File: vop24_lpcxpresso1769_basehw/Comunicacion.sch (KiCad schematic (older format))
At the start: 26 parts, among them J301 USB_B_Micro, J302 Conn_01x06_Male, J303 Conn_01x05_Male, J304 Screw_Terminal_01x02, U301 TPD4S014, U302 LTC4411, U303 LT1512

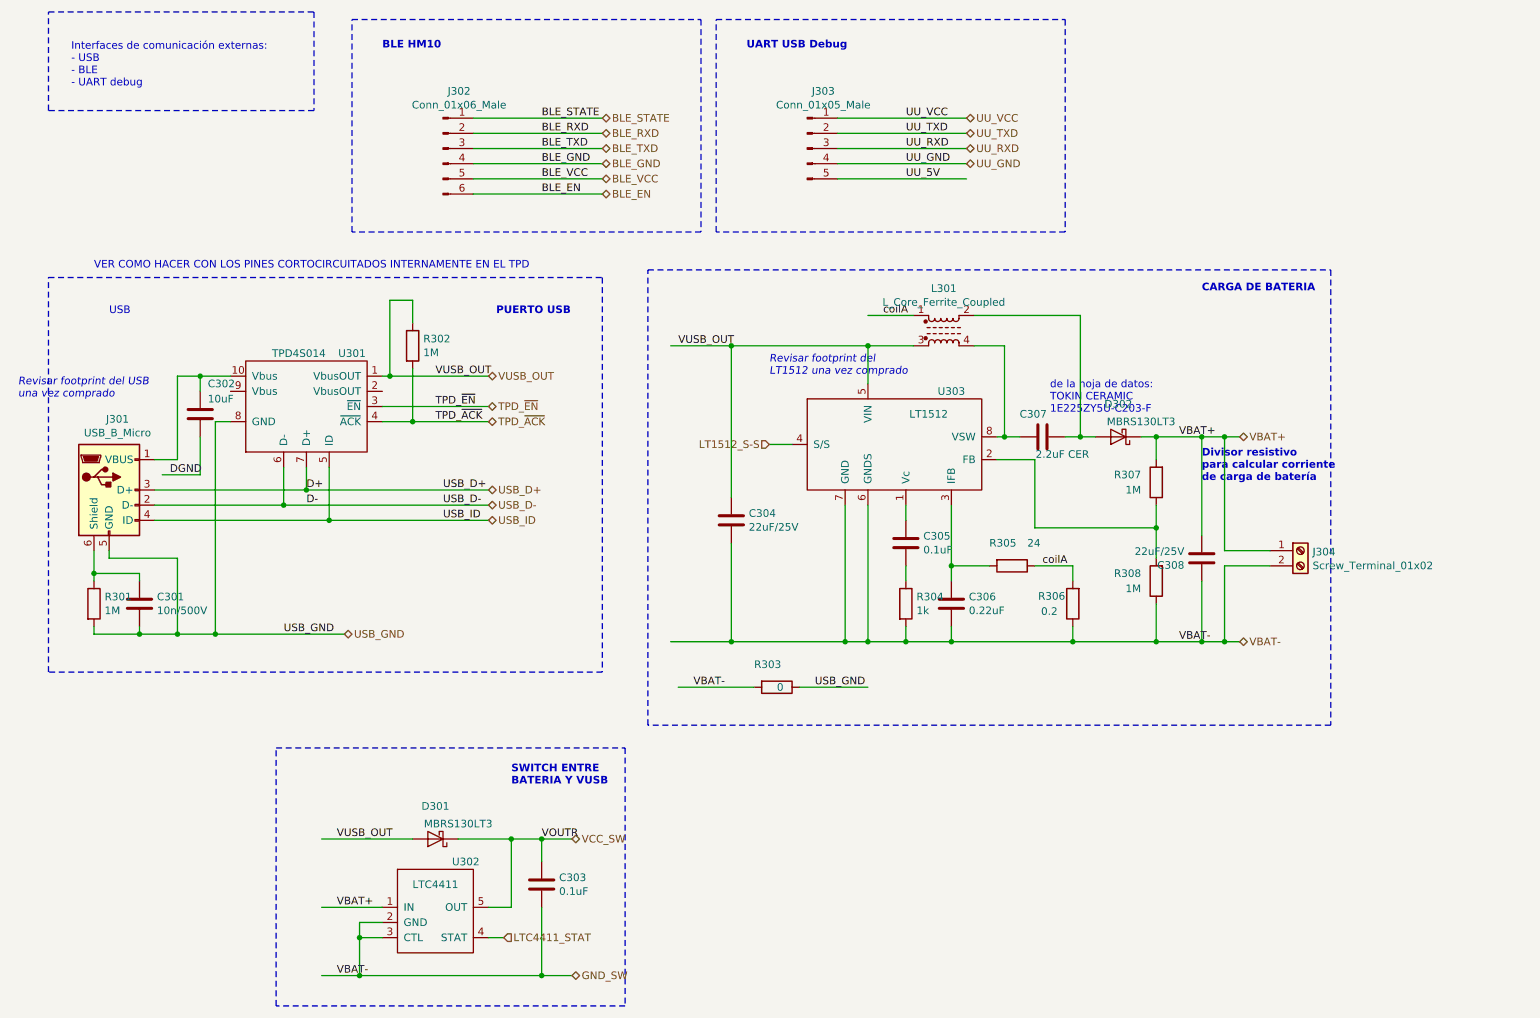
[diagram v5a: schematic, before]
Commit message: Finalizada asociación de todos los footprints. Ver librerías froux-kicad
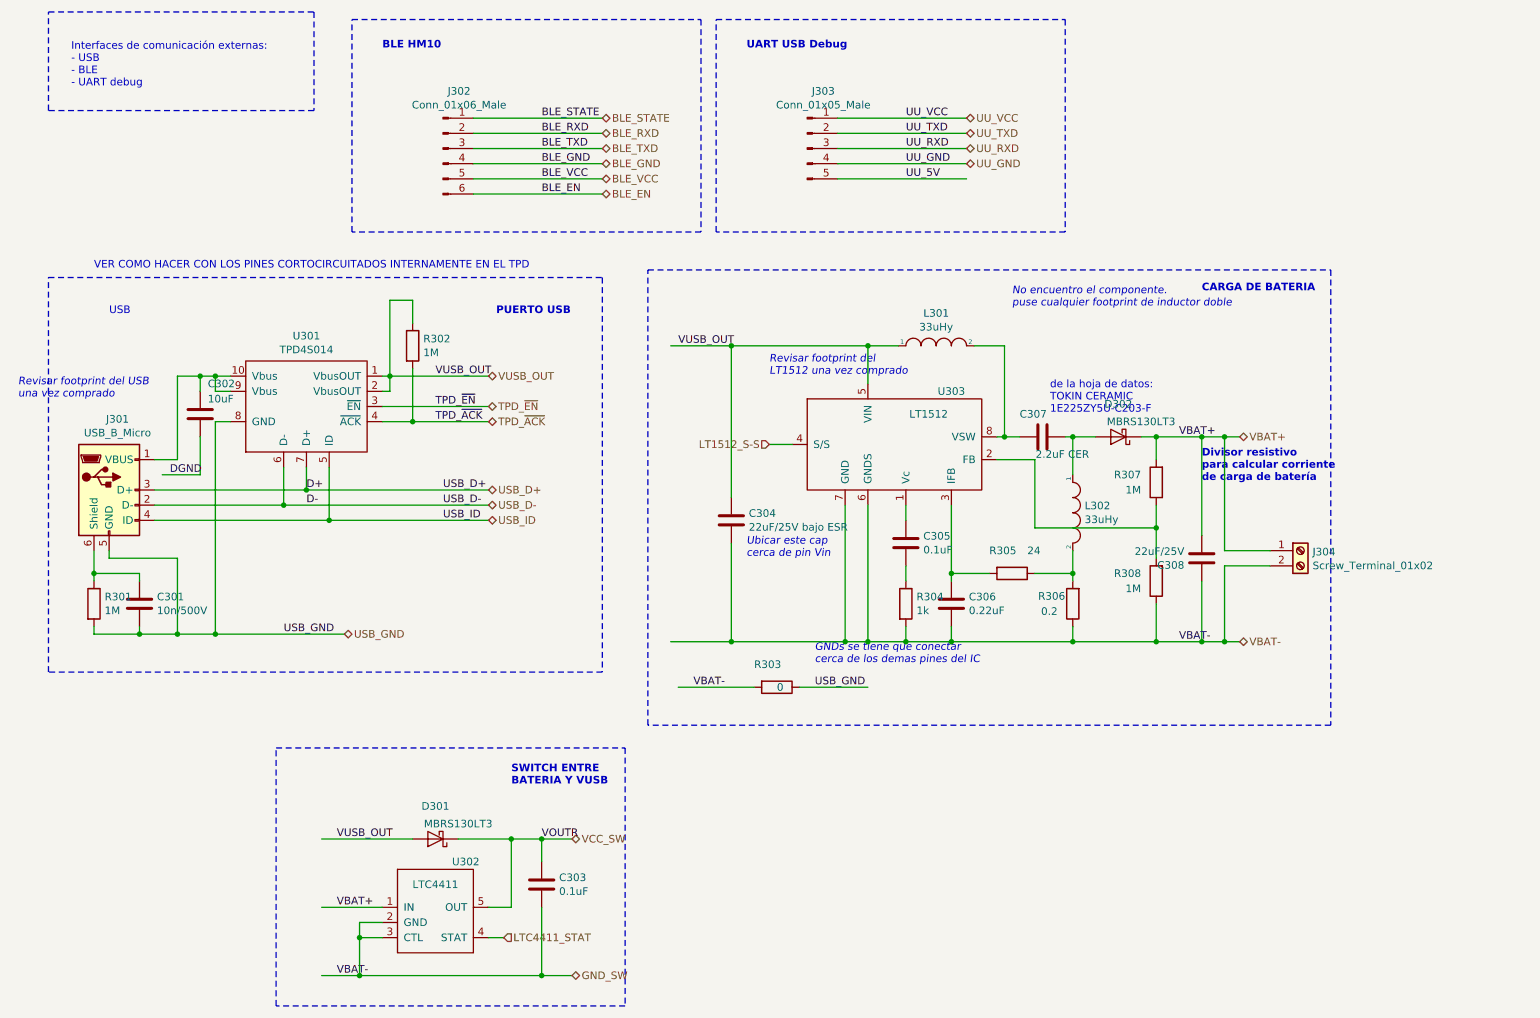
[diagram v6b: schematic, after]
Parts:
- removed L301: L_Core_Ferrite_Coupled, symbol Device:L_Core_Ferrite_Coupled
- added L301, L302: 33uHy, Inductor_THT:L_Radial_D8.7mm_P5.00mm_Fastron_07HCP, symbol pspice:INDUCTOR
- C301, C302, C303, C305, C306: footprint (none) -> Capacitor_SMD:C_0805_2012Metric_Pad1.15x1.40mm_HandSolder
- C304: value 22uF/25V -> 22uF/25V bajo ESR; footprint (none) -> Capacitor_THT:CP_Radial_D5.0mm_P2.50mm
- C307, C308: footprint (none) -> Capacitor_THT:CP_Radial_D5.0mm_P2.50mm
- D302: footprint (none) -> Diode_SMD:D_SMB-SMC_Universal_Handsoldering
- J302: footprint (none) -> Connector_PinHeader_1.27mm:PinHeader_1x06_P1.27mm_Vertical
- J303: footprint (none) -> Connector_PinHeader_1.27mm:PinHeader_1x05_P1.27mm_Vertical
- J304: footprint (none) -> TerminalBlock:TerminalBlock_bornier-2_P5.08mm
- R301, R302, R303, R304, R305, R306, R307, R308: footprint (none) -> Resistor_SMD:R_0805_2012Metric_Pad1.15x1.40mm_HandSolder
- U301: footprint Package_SON:Texas_S-PWSON-N10 -> meport_kicad_libs:Texas_R-PWSON-N10
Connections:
- net labels removed: coilA
- wire segments 125 -> 129
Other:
- note added: "GNDs se tiene que conectar\ncerca de los demas pines del IC"
- note added: "No encuentro el componente.\npuse cualquier footprint de inductor doble"
- note added: "Ubicar este cap\ncerca de pin Vin"
- moved on the sheet: R305
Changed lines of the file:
@@
 F 0 "R301" H 1070 4596 50  0000 L CNN
 F 1 "1M" H 1070 4505 50  0000 L CNN
-F 2 "" V 930 4550 50  0001 C CNN
+F 2 "Resistor_SMD:R_0805_2012Metric_Pad1.15x1.40mm_HandSolder" V 930 4550 50  0001 C CNN
 F 3 "~" H 1000 4550 50  0001 C CNN
 	1    1000 4550
@@
 F 0 "C301" H 1415 4596 50  0000 L CNN
 F 1 "10n/500V" H 1415 4505 50  0000 L CNN
-F 2 "" H 1338 4400 50  0001 C CNN
+F 2 "Capacitor_SMD:C_0805_2012Metric_Pad1.15x1.40mm_HandSolder" H 1338 4400 50  0001 C CNN
 F 3 "~" H 1300 4550 50  0001 C CNN
 	1    1300 4550
@@
 F 0 "J302" H 3406 1928 50  0000 C CNN
 F 1 "Conn_01x06_Male" H 3406 1837 50  0000 C CNN
-F 2 "" H 3300 1550 50  0001 C CNN
+F 2 "Connector_PinHeader_1.27mm:PinHeader_1x06_P1.27mm_Vertical" H 3300 1550 50  0001 C CNN
 F 3 "~" H 3300 1550 50  0001 C CNN
 	1    3300 1550
@@
 F 3 "~" H 1250 3750 50  0001 C CNN
 	1    1100 3800
-	1    0    0    -1
-$EndComp
-$Comp
-L tpd4s014:TPD4S014 U301
-U 1 1 5BAE3ACE
-P 2400 3250
-F 0 "U301" H 2700 3600 50  0000 C CNN
-F 1 "TPD4S014" H 2350 3600 50  0000 C CNN
-F 2 "Package_SON:Texas_S-PWSON-N10" H 2250 3250 50  0001 C CNN
-F 3 "/home/froux/Dropbox/VOP24/docs y hojas de datos/otros/cosas modulo usb/tpd4s014.pdf" H 2250 3250 50  0001 C CNN
-	1    2400 3250
 	1    0    0    -1
 $EndComp
@@
 F 0 "J303" H 5806 1928 50  0000 C CNN
 F 1 "Conn_01x05_Male" H 5806 1837 50  0000 C CNN
-F 2 "" H 5700 1550 50  0001 C CNN
+F 2 "Connector_PinHeader_1.27mm:PinHeader_1x05_P1.27mm_Vertical" H 5700 1550 50  0001 C CNN
 F 3 "~" H 5700 1550 50  0001 C CNN
 	1    5700 1550
@@
 F 0 "R302" H 3170 2896 50  0000 L CNN
 F 1 "1M" H 3170 2805 50  0000 L CNN
-F 2 "" V 3030 2850 50  0001 C CNN
+F 2 "Resistor_SMD:R_0805_2012Metric_Pad1.15x1.40mm_HandSolder" V 3030 2850 50  0001 C CNN
 F 3 "~" H 3100 2850 50  0001 C CNN
 	1    3100 2850
@@
 P 5200 4000
 F 0 "C304" H 5315 4046 50  0000 L CNN
-F 1 "22uF/25V" H 5315 3955 50  0000 L CNN
-F 2 "" H 5238 3850 50  0001 C CNN
+F 1 "22uF/25V bajo ESR" H 5315 3955 50  0000 L CNN
+F 2 "Capacitor_THT:CP_Radial_D5.0mm_P2.50mm" H 5238 3850 50  0001 C CNN
 F 3 "~" H 5200 4000 50  0001 C CNN
 	1    5200 4000
@@
 F 0 "C305" H 6465 4196 50  0000 L CNN
 F 1 "0.1uF" H 6465 4105 50  0000 L CNN
-F 2 "" H 6388 4000 50  0001 C CNN
+F 2 "Capacitor_SMD:C_0805_2012Metric_Pad1.15x1.40mm_HandSolder" H 6388 4000 50  0001 C CNN
 F 3 "~" H 6350 4150 50  0001 C CNN
 	1    6350 4150
@@
 F 0 "C306" H 6765 4596 50  0000 L CNN
 F 1 "0.22uF" H 6765 4505 50  0000 L CNN
-F 2 "" H 6688 4400 50  0001 C CNN
+F 2 "Capacitor_SMD:C_0805_2012Metric_Pad1.15x1.40mm_HandSolder" H 6688 4400 50  0001 C CNN
 F 3 "~" H 6650 4550 50  0001 C CNN
 	1    6650 4550
@@
 F 0 "C307" V 7100 3300 50  0000 L CNN
 F 1 "2.2uF CER" V 7365 3405 50  0000 L CNN
-F 2 "" H 7288 3300 50  0001 C CNN
+F 2 "Capacitor_THT:CP_Radial_D5.0mm_P2.50mm" H 7288 3300 50  0001 C CNN
 F 3 "~" H 7250 3450 50  0001 C CNN
 	1    7250 3450
@@
 F 0 "C308" H 8415 4296 50  0000 L CNN
 F 1 "22uF/25V" H 8415 4205 50  0000 L CNN
-F 2 "" H 8338 4100 50  0001 C CNN
+F 2 "Capacitor_THT:CP_Radial_D5.0mm_P2.50mm" H 8338 4100 50  0001 C CNN
 F 3 "~" H 8300 4250 50  0001 C CNN
 	1    8300 4250
@@
 F 0 "R304" H 6420 4596 50  0000 L CNN
 F 1 "1k" H 6420 4505 50  0000 L CNN
-F 2 "" V 6280 4550 50  0001 C CNN
+F 2 "Resistor_SMD:R_0805_2012Metric_Pad1.15x1.40mm_HandSolder" V 6280 4550 50  0001 C CNN
 F 3 "~" H 6350 4550 50  0001 C CNN
 	1    6350 4550
@@
 F 0 "R306" H 7500 4500 50  0000 L CNN
 F 1 "0.2" H 7550 4600 50  0000 L CNN
-F 2 "" V 7380 4550 50  0001 C CNN
+F 2 "Resistor_SMD:R_0805_2012Metric_Pad1.15x1.40mm_HandSolder" V 7380 4550 50  0001 C CNN
 F 3 "~" H 7450 4550 50  0001 C CNN
 	1    7450 4550
@@
 L Device:R R305
 U 1 1 5BC35500
-P 7050 4300
-F 0 "R305" V 6900 4150 50  0000 L CNN
-F 1 "24" V 6900 4400 50  0000 L CNN
-F 2 "" V 6980 4300 50  0001 C CNN
-F 3 "~" H 7050 4300 50  0001 C CNN
-	1    7050 4300
+P 7050 4350
+F 0 "R305" V 6900 4200 50  0000 L CNN
+F 1 "24" V 6900 4450 50  0000 L CNN
+F 2 "Resistor_SMD:R_0805_2012Metric_Pad1.15x1.40mm_HandSolder" V 6980 4350 50  0001 C CNN
+F 3 "~" H 7050 4350 50  0001 C CNN
+	1    7050 4350
 	0    1    1    0
 $EndComp
@@
 F 0 "R307" H 8100 3700 50  0000 L CNN
 F 1 "1M" H 8100 3800 50  0000 L CNN
-F 2 "" V 7930 3750 50  0001 C CNN
+F 2 "Resistor_SMD:R_0805_2012Metric_Pad1.15x1.40mm_HandSolder" V 7930 3750 50  0001 C CNN
 F 3 "~" H 8000 3750 50  0001 C CNN
 	1    8000 3750
@@
 F 0 "R308" H 8100 4350 50  0000 L CNN
 F 1 "1M" H 8100 4450 50  0000 L CNN
-F 2 "" V 7930 4400 50  0001 C CNN
+F 2 "Resistor_SMD:R_0805_2012Metric_Pad1.15x1.40mm_HandSolder" V 7930 4400 50  0001 C CNN
 F 3 "~" H 8000 4400 50  0001 C CNN
 	1    8000 4400
@@
 Text Notes 8300 3750 0    50   ~ 10
 Divisor resistivo\npara calcular corriente\nde carga de batería
-$Comp
-L Device:L_Core_Ferrite_Coupled L301
-U 1 1 5BC35BED
-P 6600 2750
-F 0 "L301" H 6600 3028 50  0000 C CNN
-F 1 "L_Core_Ferrite_Coupled" H 6600 2937 50  0000 C CNN
-F 2 "" H 6600 2750 50  0001 C CNN
-F 3 "~" H 6600 2750 50  0001 C CNN
-	1    6600 2750
-	1    0    0    -1
-$EndComp
-Wire Wire Line
-	6400 2850 6100 2850
+Wire Wire Line
+	6300 2850 6100 2850
 Wire Wire Line
 	5200 2850 5200 3850
@@
 	6350 4400 6350 4300
 Wire Wire Line
-	6650 4400 6650 4300
-Wire Wire Line
-	6650 4300 6900 4300
-Connection ~ 6650 4300
-Wire Wire Line
-	6650 4300 6650 3900
-Wire Wire Line
-	7200 4300 7450 4300
-Wire Wire Line
-	7450 4300 7450 4400
+	6650 4400 6650 4350
+Wire Wire Line
+	6650 4350 6900 4350
+Connection ~ 6650 4350
+Wire Wire Line
+	6650 4350 6650 3900
+Wire Wire Line
+	7200 4350 7450 4350
+Wire Wire Line
+	7450 4350 7450 4400
 Wire Wire Line
 	8000 4250 8000 4050
@@
 	8000 4050 8000 3900
 Wire Wire Line
-	6800 2650 7500 2650
-Wire Wire Line
-	7500 3450 7400 3450
-Wire Wire Line
-	7500 2650 7500 3450
-Wire Wire Line
 	7450 4800 8000 4800
 Wire Wire Line
@@
 Wire Wire Line
 	8000 4800 8300 4800
-Wire Wire Line
-	6400 2650 6100 2650
-Text Label 6200 2650 0    50   ~ 0
-coilA
-Text Label 7250 4300 0    50   ~ 0
-coilA
 $Comp
 L Device:D_Schottky D302
@@
 F 0 "D302" H 7750 3234 50  0000 C CNN
 F 1 "MBRS130LT3" H 7600 3350 50  0000 C CNN
-F 2 "" H 7750 3450 50  0001 C CNN
+F 2 "Diode_SMD:D_SMB-SMC_Universal_Handsoldering" H 7750 3450 50  0001 C CNN
 F 3 "~" H 7750 3450 50  0001 C CNN
 	1    7750 3450
 	-1   0    0    1
 $EndComp
-Wire Wire Line
-	7600 3450 7500 3450
-Connection ~ 7500 3450
 Wire Wire Line
 	7900 3450 8000 3450
@@
 F 0 "C303" H 4065 6446 50  0000 L CNN
 F 1 "0.1uF" H 4065 6355 50  0000 L CNN
-F 2 "" H 3988 6250 50  0001 C CNN
+F 2 "Capacitor_SMD:C_0805_2012Metric_Pad1.15x1.40mm_HandSolder" H 3988 6250 50  0001 C CNN
 F 3 "~" H 3950 6400 50  0001 C CNN
 	1    3950 6400
@@
 F 0 "R303" V 5350 4950 50  0000 L CNN
 F 1 "0" V 5500 5100 50  0000 L CNN
-F 2 "" V 5430 5100 50  0001 C CNN
+F 2 "Resistor_SMD:R_0805_2012Metric_Pad1.15x1.40mm_HandSolder" V 5430 5100 50  0001 C CNN
 F 3 "~" H 5500 5100 50  0001 C CNN
 	1    5500 5100
@@
 F 0 "C302" H 1750 3500 50  0000 L CNN
 F 1 "10uF" H 1750 3400 50  0000 L CNN
-F 2 "" H 1738 3150 50  0001 C CNN
+F 2 "Capacitor_SMD:C_0805_2012Metric_Pad1.15x1.40mm_HandSolder" H 1738 3150 50  0001 C CNN
 F 3 "~" H 1700 3300 50  0001 C CNN
 	1    1700 3300
@@
 Connection ~ 1700 3050
 Wire Wire Line
-	1700 3050 1900 3050
+	1700 3050 1800 3050
 Wire Notes Line
 	9150 2350 9150 5350
@@
 F 0 "J304" H 9030 4192 50  0000 L CNN
 F 1 "Screw_Terminal_01x02" H 9030 4101 50  0000 L CNN
-F 2 "" H 8950 4200 50  0001 C CNN
+F 2 "TerminalBlock:TerminalBlock_bornier-2_P5.08mm" H 8950 4200 50  0001 C CNN
 F 3 "~" H 8950 4200 50  0001 C CNN
 	1    8950 4200
@@
 Text Notes 5450 3050 0    50   Italic 0
 Revisar footprint del \nLT1512 una vez comprado
+Text Notes 7050 2600 0    50   Italic 0
+No encuentro el componente.\npuse cualquier footprint de inductor doble
+Text Notes 5300 4250 0    50   Italic 0
+Ubicar este cap\ncerca de pin Vin
+Text Notes 5750 4950 0    50   Italic 0
+GNDs se tiene que conectar\ncerca de los demas pines del IC
+$Comp
+L pspice:INDUCTOR L302
+U 1 1 5BD9F38A
+P 7450 3950
+F 0 "L302" V 7404 4028 50  0000 L CNN
+F 1 "33uHy" V 7495 4028 50  0000 L CNN
+F 2 "Inductor_THT:L_Radial_D8.7mm_P5.00mm_Fastron_07HCP" H 7450 3950 50  0001 C CNN
+F 3 "" H 7450 3950 50  0001 C CNN
+	1    7450 3950
+	0    1    1    0
+$EndComp
+$Comp
+L pspice:INDUCTOR L301
+U 1 1 5BD9F433
+P 6550 2850
+F 0 "L301" H 6550 3065 50  0000 C CNN
+F 1 "33uHy" H 6550 2974 50  0000 C CNN
+F 2 "Inductor_THT:L_Radial_D8.7mm_P5.00mm_Fastron_07HCP" H 6550 2850 50  0001 C CNN
+F 3 "" H 6550 2850 50  0001 C CNN
+	1    6550 2850
+	1    0    0    -1
+$EndComp
+Wire Wire Line
+	7400 3450 7450 3450
+Wire Wire Line
+	7450 4200 7450 4350
+Connection ~ 7450 4350
+Wire Wire Line
+	7450 3700 7450 3450
+Connection ~ 7450 3450
+Wire Wire Line
+	7450 3450 7600 3450
+$Comp
+L tpd4s014:TPD4S014 U301
+U 1 1 5BDBF51B
+P 2400 3250
+F 0 "U301" H 2400 3715 50  0000 C CNN
+F 1 "TPD4S014" H 2400 3624 50  0000 C CNN
+F 2 "meport_kicad_libs:Texas_R-PWSON-N10" H 2250 3250 50  0001 C CNN
+F 3 "/home/froux/Dropbox/VOP24/docs y hojas de datos/otros/cosas modulo usb/tpd4s014.pdf" H 2250 3250 50  0001 C CNN
+	1    2400 3250
+	1    0    0    -1
+$EndComp
+Wire Wire Line
+	1900 3150 1800 3150
+Wire Wire Line
+	1800 3150 1800 3050
+Connection ~ 1800 3050
+Wire Wire Line
+	1800 3050 1900 3050
+Wire Wire Line
+	2900 3150 2950 3150
+Wire Wire Line
+	2950 3150 2950 3050
 $EndSCHEMATC

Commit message: Primer commit sobre el diseño del PCB. Se agruparon algunas hojas de esquemáticos. No se empezó a rutear
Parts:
- J302: footprint Connector_PinHeader_1.27mm:PinHeader_1x06_P1.27mm_Vertical -> Connector_PinSocket_2.54mm:PinSocket_1x06_P2.54mm_Vertical
- J303: footprint Connector_PinHeader_1.27mm:PinHeader_1x05_P1.27mm_Vertical -> Connector_PinSocket_2.54mm:PinSocket_1x05_P2.54mm_Vertical
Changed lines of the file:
@@
 F 0 "J302" H 3406 1928 50  0000 C CNN
 F 1 "Conn_01x06_Male" H 3406 1837 50  0000 C CNN
-F 2 "Connector_PinHeader_1.27mm:PinHeader_1x06_P1.27mm_Vertical" H 3300 1550 50  0001 C CNN
+F 2 "Connector_PinSocket_2.54mm:PinSocket_1x06_P2.54mm_Vertical" H 3300 1550 50  0001 C CNN
 F 3 "~" H 3300 1550 50  0001 C CNN
 	1    3300 1550
@@
 F 0 "J303" H 5806 1928 50  0000 C CNN
 F 1 "Conn_01x05_Male" H 5806 1837 50  0000 C CNN
-F 2 "Connector_PinHeader_1.27mm:PinHeader_1x05_P1.27mm_Vertical" H 5700 1550 50  0001 C CNN
+F 2 "Connector_PinSocket_2.54mm:PinSocket_1x05_P2.54mm_Vertical" H 5700 1550 50  0001 C CNN
 F 3 "~" H 5700 1550 50  0001 C CNN
 	1    5700 1550

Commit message: PCB: posicionamiento preruteo. ESQ: cambio de footprint de conectores
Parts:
- J301: symbol Connector:USB_B_Micro -> vop24_lpcxpresso1769_basehw-rescue:USB_B_Micro-Connector
- J302: symbol Connector:Conn_01x06_Male -> vop24_lpcxpresso1769_basehw-rescue:Conn_01x06_Male-Connector
- J303: symbol Connector:Conn_01x05_Male -> vop24_lpcxpresso1769_basehw-rescue:Conn_01x05_Male-Connector
- J304: symbol Connector:Screw_Terminal_01x02 -> vop24_lpcxpresso1769_basehw-rescue:Screw_Terminal_01x02-Connector
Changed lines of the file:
@@
 	1550 4250 1550 4750
 $Comp
-L Connector:Conn_01x06_Male J302
+L vop24_lpcxpresso1769_basehw-rescue:Conn_01x06_Male-Connector J302
 U 1 1 5BA01F94
 P 3300 1550
@@
 	1400 3800 2400 3800
 $Comp
-L Connector:USB_B_Micro J301
+L vop24_lpcxpresso1769_basehw-rescue:USB_B_Micro-Connector J301
 U 1 1 5BAE3529
 P 1100 3800
+AR Path="/5BAE3529" Ref="J301"  Part="1"
+AR Path="/5B9DAB38/5BAE3529" Ref="J301"  Part="1"
 F 0 "J301" H 1155 4267 50  0000 C CNN
 F 1 "USB_B_Micro" H 1155 4176 50  0000 C CNN
@@
 UU_VCC
 $Comp
-L Connector:Conn_01x05_Male J303
+L vop24_lpcxpresso1769_basehw-rescue:Conn_01x05_Male-Connector J303
 U 1 1 5BAF1C86
 P 5700 1550
+AR Path="/5BAF1C86" Ref="J303"  Part="1"
+AR Path="/5B9DAB38/5BAF1C86" Ref="J303"  Part="1"
 F 0 "J303" H 5806 1928 50  0000 C CNN
 F 1 "Conn_01x05_Male" H 5806 1837 50  0000 C CNN
@@
 GND_SW
 $Comp
-L Connector:Screw_Terminal_01x02 J304
+L vop24_lpcxpresso1769_basehw-rescue:Screw_Terminal_01x02-Connector J304
 U 1 1 5BDFE4B3
 P 8950 4200
+AR Path="/5BDFE4B3" Ref="J304"  Part="1"
+AR Path="/5B9DAB38/5BDFE4B3" Ref="J304"  Part="1"
 F 0 "J304" H 9030 4192 50  0000 L CNN
 F 1 "Screw_Terminal_01x02" H 9030 4101 50  0000 L CNN
